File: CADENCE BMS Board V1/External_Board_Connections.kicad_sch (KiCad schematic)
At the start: 44 parts, among them J10 Conn_01x08, J11 Conn_01x06, J12 Conn_01x02, J13 Conn_01x08, J14 Conn_01x04, J15 Conn_01x08, J2 Conn_01x02, J27 USB_C_Receptacle_USB2.0_16P, J29 Conn_01x02, J3 Conn_01x08, J30 Conn_01x02, J4 Conn_01x02, J5 Conn_01x01_Socket, J6 Conn_01x01_Socket, J7 Conn_01x01_Socket, J8 Conn_01x01_Socket, J9 Conn_01x04, Q27 Q_PMOS_DGS, Q28 Q_PMOS_DGS, U11 CYPD3177-24LQ

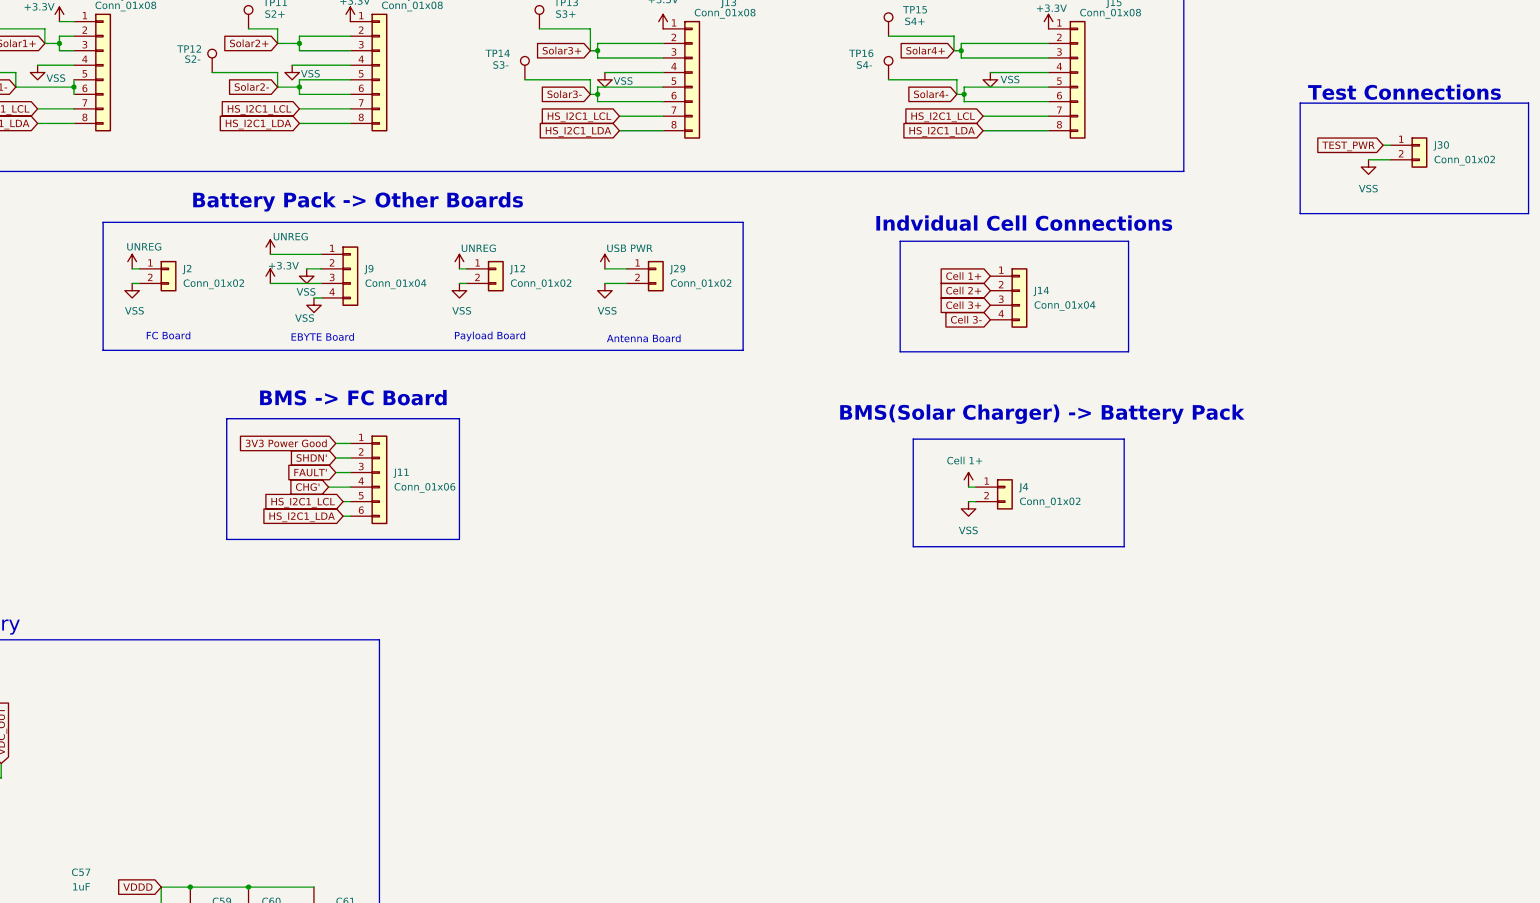
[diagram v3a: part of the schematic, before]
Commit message: Updates to incorporate inhibit board
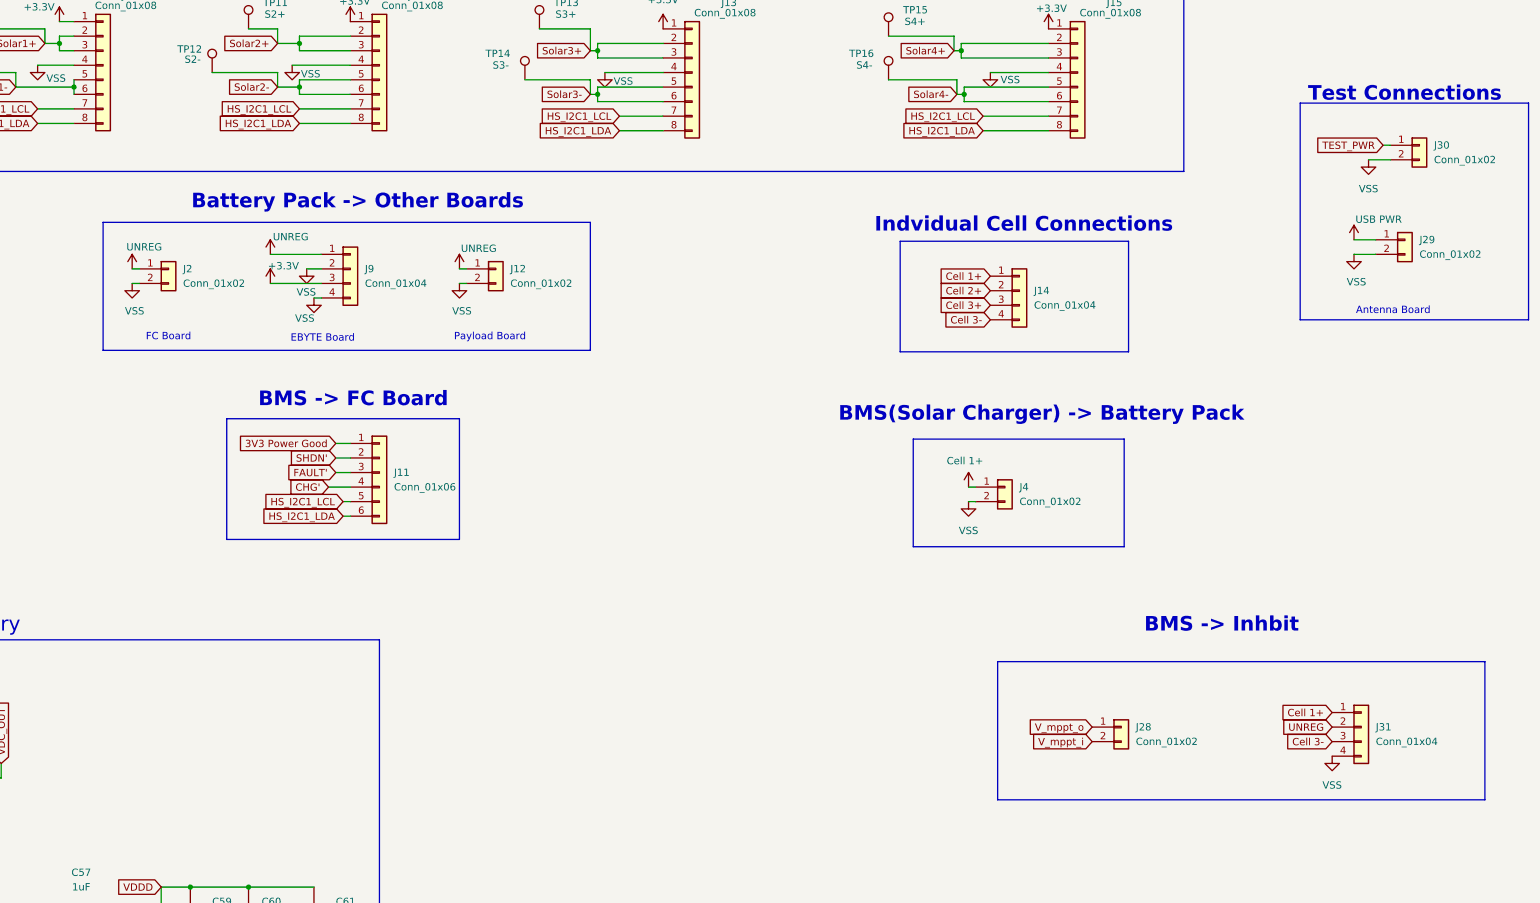
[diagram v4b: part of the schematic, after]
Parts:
- added J28: Conn_01x02, Connector_JST:JST_XH_B2B-XH-A_1x02_P2.50mm_Vertical, symbol Connector_Generic:Conn_01x02
- added J31: Conn_01x04, Connector_JST:JST_XH_B4B-XH-A_1x04_P2.50mm_Vertical, symbol Connector_Generic:Conn_01x04
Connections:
- net Cell 1+: now also J31.1 (Pin_1)
- net Cell 3-: now also J31.3 (Pin_3)
- net UNREG: now also J31.2 (Pin_2)
- net VSS: now also J31.4 (Pin_4)
- new net V_mppt_i: J28.2 (Pin_2)
- new net V_mppt_o: J28.1 (Pin_1)
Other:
- note added: "BMS -> Inhbit"
- moved on the sheet: J29

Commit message: Updates to finalize V1
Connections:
- net Solar1- is gone; now on net VSS: J10.5 (Pin_5), J10.6 (Pin_6), J13.5 (Pin_5), J13.6 (Pin_6), J15.5 (Pin_5), J15.6 (Pin_6), J3.5 (Pin_5), J3.6 (Pin_6), TP12.1, TP14.1, TP16.1, TP9.1
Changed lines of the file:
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@@
 	(wire
 		(pts
-			(xy 74.93 115.57) (xy 74.93 130.81)
-		)
-		(stroke
-			(width 0)
-			(type default)
-		)
-	)
-	(wire
-		(pts
 			(xy 132.08 240.03) (xy 137.16 240.03)
 		)
@@
 	(wire
 		(pts
+			(xy 74.93 132.08) (xy 76.2 132.08)
+		)
+		(stroke
+			(width 0)
+			(type default)
+		)
+	)
+	(wire
+		(pts
 			(xy 298.45 53.34) (xy 287.02 53.34)
 		)
@@
 	(wire
 		(pts
+			(xy 74.93 115.57) (xy 74.93 132.08)
+		)
+		(stroke
+			(width 0)
+			(type default)
+		)
+	)
+	(wire
+		(pts
 			(xy 168.91 59.69) (xy 180.34 59.69)
 		)
@@
 					(unit 1)
 				)
+			)
+		)
+	)
+	(symbol
+		(lib_id "power:GND")
+		(at 76.2 132.08 0)
+		(unit 1)
+		(body_style 1)
+		(exclude_from_sim no)
+		(in_bom yes)
+		(on_board yes)
+		(in_pos_files yes)
+		(dnp no)
+		(property "Reference" "#PWR083"
+			(at 76.2 138.43 0)
+			(hide yes)
+			(show_name no)
+			(do_not_autoplace no)
+			(effects
+				(font
+					(size 1.27 1.27)
+				)
+			)
+		)
+		(property "Value" "VSS"
+			(at 74.93 136.906 0)
+			(show_name no)
+			(do_not_autoplace no)
+			(effects
+				(font
+					(size 1.27 1.27)
+				)
+				(justify left)
+			)
+		)
+		(property "Footprint" ""
+			(at 76.2 132.08 0)
+			(hide yes)
+			(show_name no)
+			(do_not_autoplace no)
+			(effects
+				(font
+					(size 1.27 1.27)
+				)
+			)
+		)
+		(property "Datasheet" ""
+			(at 76.2 132.08 0)
+			(hide yes)
+			(show_name no)
+			(do_not_autoplace no)
+			(effects
+				(font
+					(size 1.27 1.27)
+				)
+			)
+		)
+		(property "Description" "Power symbol creates a global label with name \"GND\" , ground"
+			(at 76.2 132.08 0)
+			(hide yes)
+			(show_name no)
+			(do_not_autoplace no)
+			(effects
+				(font
+					(size 1.27 1.27)
+				)
+			)
+		)
+		(pin "1"
+		)
+		(instances
+			(project "BMS_Board_Prototype"
+				(path "/4ee99911-836b-4752-8a2d-327c8b28dc47/420608bc-a1a4-412d-a20e-6570cff27a90"
+					(reference "#PWR083")
+					(unit 1)
+				)

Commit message: Updates for connector footprint
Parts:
- J14: footprint Connector_JST:JST_NV_B04P-NV_1x04_P5.00mm_Vertical -> Connector_Samtec_HPM_THT:Samtec_HPM-04-05-x-S_Straight_1x04_Pitch5.08mm
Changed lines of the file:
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@@
 			)
 		)
-		(property "Footprint" "Connector_JST:JST_NV_B04P-NV_1x04_P5.00mm_Vertical"
+		(property "Footprint" "Connector_Samtec_HPM_THT:Samtec_HPM-04-05-x-S_Straight_1x04_Pitch5.08mm"
 			(at 309.88 97.79 0)
 			(hide yes)

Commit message: Fabrication Files
Adding in the files need for the fabrication of the PCB. Used the interactive BOM and the JLC addition tool to add in components
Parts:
- C43: footprint Diode_SMD:D_SOD-123 -> Capacitor_SMD:C_0805_2012Metric
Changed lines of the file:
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@@
 			)
 		)
-		(property "Footprint" "Diode_SMD:D_SOD-123"
+		(property "Footprint" "Capacitor_SMD:C_0805_2012Metric"
 			(at 74.93 82.8548 0)
 			(hide yes)

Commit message: Updates to buried Vias and Minor Fixes
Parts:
- added TP24: C1+, TestPoint:TestPoint_THTPad_D1.0mm_Drill0.5mm, symbol Connector:TestPoint
- added TP25: C2+, TestPoint:TestPoint_THTPad_D1.0mm_Drill0.5mm, symbol Connector:TestPoint
- added TP26: C3+, TestPoint:TestPoint_THTPad_D1.0mm_Drill0.5mm, symbol Connector:TestPoint
- added TP27: C3-, TestPoint:TestPoint_THTPad_D1.0mm_Drill0.5mm, symbol Connector:TestPoint
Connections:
- net Cell 1+: now also TP24.1
- net Cell 2+: now also TP25.1
- net Cell 3+: now also TP26.1
- net Cell 3-: now also TP27.1
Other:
- note added: "Cell Test Points"
